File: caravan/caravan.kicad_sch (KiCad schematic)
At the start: 61 parts

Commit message: updated caravan
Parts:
- R?: value 680Ω -> 47Ω
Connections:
- new net: CB?.1, U?. (PE), U?.~ (PE)
- new net: CB?.3, U?. (PE), U?.~ (PE)
- new net: U?. (OUT-), U?. (PE) (x2)
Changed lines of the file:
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@@
   (title_block
     (title "Autark-Schaltplan")
-    (date "2024-10-14")
+    (date "2024-11-29")
     (comment 1 "Fendt Bianco Activ 390 FHS Autark-Schaltplan")
   )
@@
       (effects (font (size 1.27 1.27)) hide)
     )
-    (property "Value" "680Ω" (id 1) (at 304.165 211.1812 90))
+    (property "Value" "47Ω" (id 1) (at 304.165 211.1812 90))
     (property "Footprint" "" (id 2) (at 304.165 211.582 90)
       (effects (font (size 1.27 1.27)) hide)
@@
     )
     (path "/4729930f-060c-4c53-b9ff-46eeef07ff5b"
-      (reference "R?") (unit 1) (value "680Ω") (footprint "")
+      (reference "R?") (unit 1) (value "47Ω") (footprint "")
     )
     (path "/00000000-0000-0000-0000-000060e629cb"

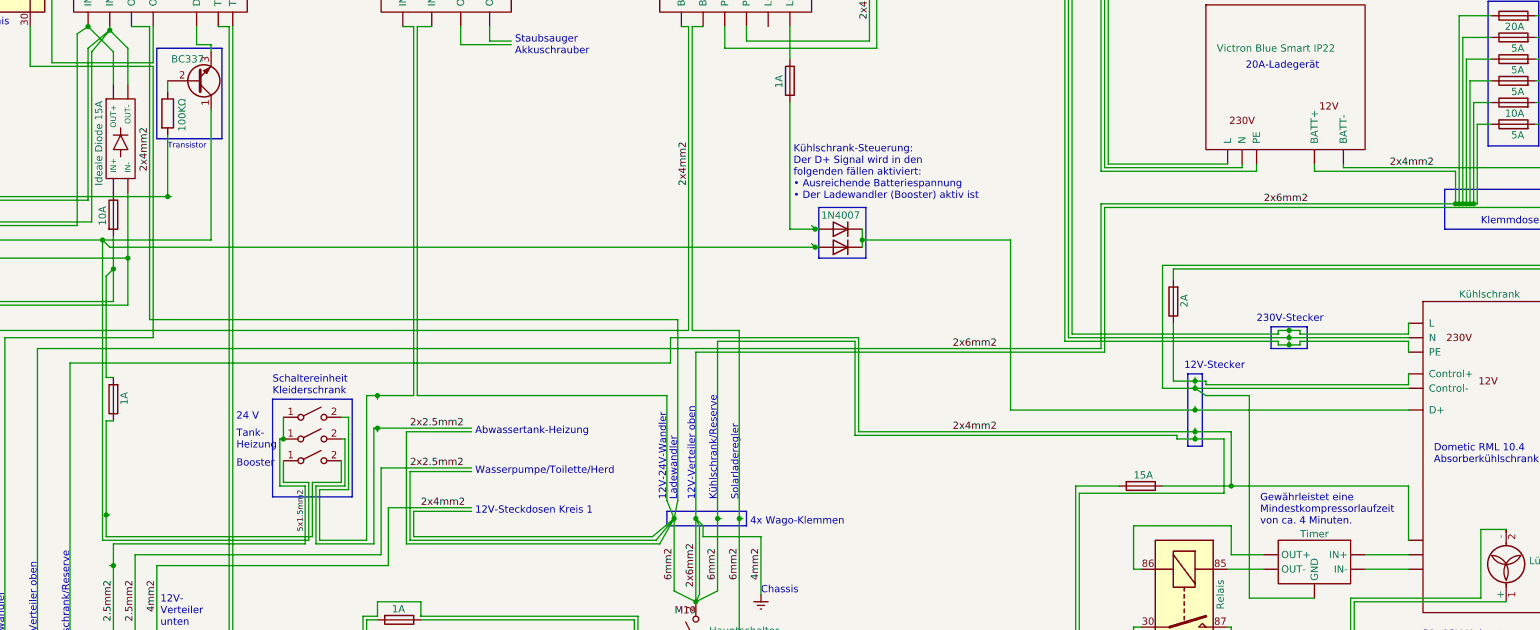
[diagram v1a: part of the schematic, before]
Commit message: Added 555-delay-opto
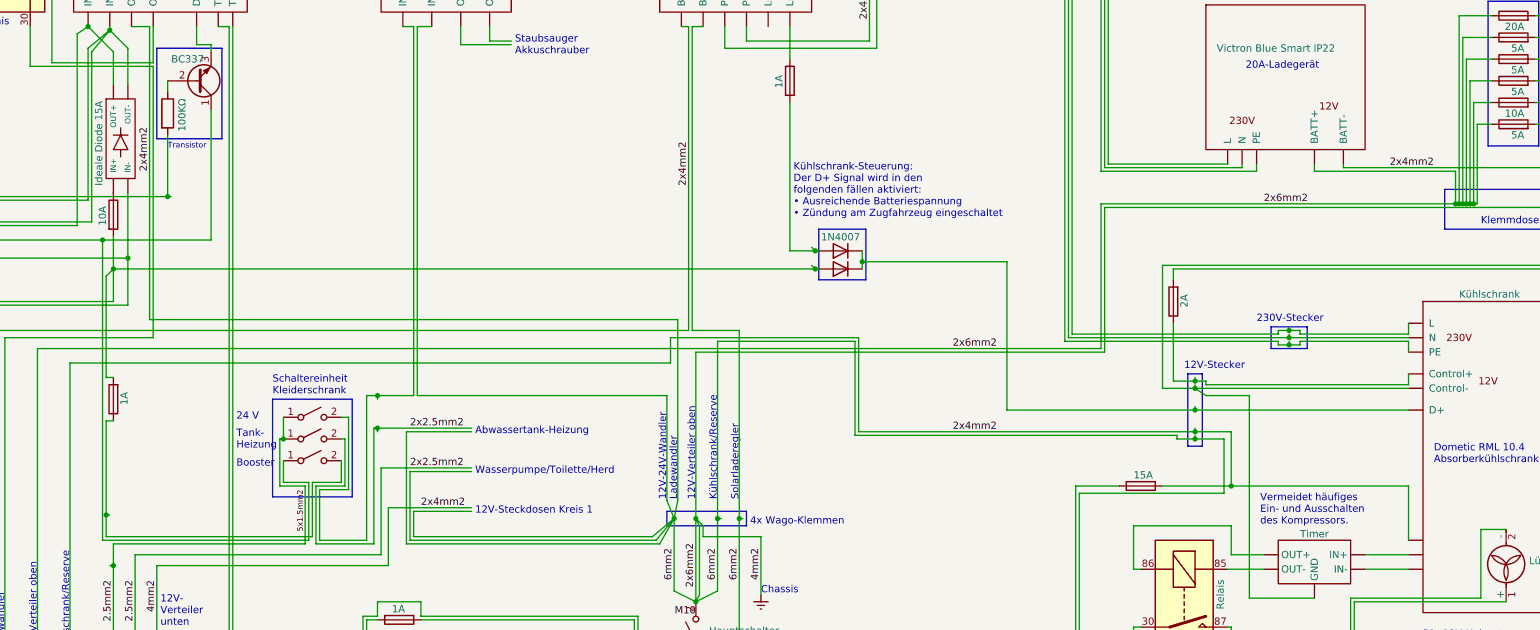
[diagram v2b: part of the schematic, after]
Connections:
- net Earth: now also D?.2 (A)
- net at K?.85, Q?.1 (C), SW?.1 (A): no longer D?.2 (A)
- new net: CB?.1, U?. (PE), U?.~ (PE)
- new net: CB?.3, U?. (PE), U?.~ (PE)
- new net: U?. (OUT-), U?. (PE) (x2)
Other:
- note added: "Kühlschrank-Steuerung: Der D+ Signal wird in den folgenden fällen aktiviert: • Ausreichende Batteriespannung • Zündung am Zugfahrzeug eingeschaltet"
- note added: "Vermeidet häufiges Ein- und Ausschalten des Kompressors."
- note removed: "Gewährleistet eine Mindestkompressorlaufzeit von ca. 4 Minuten."
- note removed: "Kühlschrank-Steuerung: Der D+ Signal wird in den folgenden fällen aktiviert: • Ausreichende Batteriespannung • Der Ladewandler (Booster) aktiv ist"
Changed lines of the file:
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@@
   (title_block
     (title "Autark-Schaltplan")
-    (date "2024-11-29")
+    (date "2025-01-06")
     (comment 1 "Fendt Bianco Activ 390 FHS Autark-Schaltplan")
   )
@@
   (junction (at 290.195 81.28) (diameter 0) (color 0 0 0 0)
   )
-  (junction (at 247.65 136.525) (diameter 0) (color 0 0 0 0)
+  (junction (at 247.65 140.335) (diameter 0) (color 0 0 0 0)
   )
   (junction (at 160.655 213.995) (diameter 0) (color 0 0 0 0)
@@
   (junction (at 146.05 171.45) (diameter 0) (color 0 0 0 0)
   )
-  (junction (at 239.395 137.795) (diameter 0) (color 0 0 0 0)
+  (junction (at 239.395 141.605) (diameter 0) (color 0 0 0 0)
   )
   (junction (at 108.585 212.725) (diameter 0) (color 0 0 0 0)
@@
   (junction (at 170.18 236.855) (diameter 0) (color 0 0 0 0)
   )
-  (junction (at 239.395 134.62) (diameter 0) (color 0 0 0 0)
+  (junction (at 239.395 138.43) (diameter 0) (color 0 0 0 0)
   )
   (junction (at 354.33 130.175) (diameter 0) (color 0 0 0 0)
@@
     (stroke (width 0) (type default) (color 0 0 0 0))
   )
-  (wire (pts (xy 238.76 137.16) (xy 239.395 137.795))
+  (wire (pts (xy 238.76 140.97) (xy 239.395 141.605))
     (stroke (width 0) (type default) (color 0 0 0 0))
   )
@@
     (stroke (width 0) (type default) (color 0 0 0 0))
   )
-  (wire (pts (xy 115.57 137.795) (xy 239.395 137.795))
-    (stroke (width 0) (type default) (color 0 0 0 0))
-  )
   (wire (pts (xy 332.74 213.36) (xy 332.74 213.995))
     (stroke (width 0) (type default) (color 0 0 0 0))
@@
     (stroke (width 0) (type default) (color 0 0 0 0))
   )
-  (wire (pts (xy 234.95 112.395) (xy 234.95 134.62))
+  (wire (pts (xy 234.95 112.395) (xy 234.95 138.43))
     (stroke (width 0) (type default) (color 0 0 0 0))
   )
@@
     (stroke (width 0) (type default) (color 0 0 0 0))
   )
-  (wire (pts (xy 273.685 136.525) (xy 273.685 166.37))
+  (wire (pts (xy 273.05 140.335) (xy 273.05 166.37))
     (stroke (width 0) (type default) (color 0 0 0 0))
   )
@@
     (stroke (width 0) (type default) (color 0 0 0 0))
   )
-  (wire (pts (xy 247.65 136.525) (xy 247.65 137.795))
+  (wire (pts (xy 247.65 140.335) (xy 247.65 141.605))
     (stroke (width 0) (type default) (color 0 0 0 0))
   )
@@
     (stroke (width 0) (type default) (color 0 0 0 0))
   )
-  (wire (pts (xy 273.685 166.37) (xy 306.07 166.37))
+  (wire (pts (xy 273.05 166.37) (xy 306.07 166.37))
     (stroke (width 0) (type default) (color 0 0 0 0))
   )
@@
     (stroke (width 0) (type default) (color 0 0 0 0))
   )
-  (wire (pts (xy 247.65 136.525) (xy 273.685 136.525))
+  (wire (pts (xy 247.65 140.335) (xy 273.05 140.335))
     (stroke (width 0) (type default) (color 0 0 0 0))
   )
@@
     (stroke (width 0) (type default) (color 0 0 0 0))
   )
+  (wire (pts (xy 116.205 141.605) (xy 239.395 141.605))
+    (stroke (width 0) (type default) (color 0 0 0 0))
+  )
   (wire (pts (xy 109.855 100.33) (xy 109.855 133.985))
     (stroke (width 0) (type default) (color 0 0 0 0))
@@
     (stroke (width 0) (type default) (color 0 0 0 0))
   )
-  (wire (pts (xy 247.65 134.62) (xy 247.65 136.525))
+  (wire (pts (xy 247.65 138.43) (xy 247.65 140.335))
     (stroke (width 0) (type default) (color 0 0 0 0))
   )
@@
     (stroke (width 0) (type default) (color 0 0 0 0))
   )
-  (wire (pts (xy 114.3 136.525) (xy 115.57 137.795))
-    (stroke (width 0) (type default) (color 0 0 0 0))
-  )
   (wire (pts (xy 222.25 154.305) (xy 246.38 154.305))
     (stroke (width 0) (type default) (color 0 0 0 0))
@@
     (stroke (width 0) (type default) (color 0 0 0 0))
   )
-  (polyline (pts (xy 240.03 130.81) (xy 240.03 139.7))
+  (polyline (pts (xy 240.03 134.62) (xy 240.03 143.51))
     (stroke (width 0) (type default) (color 0 0 0 0))
   )
@@
     (stroke (width 0) (type default) (color 0 0 0 0))
   )
-  (polyline (pts (xy 248.285 130.81) (xy 248.285 139.7))
+  (polyline (pts (xy 248.285 134.62) (xy 248.285 143.51))
     (stroke (width 0) (type default) (color 0 0 0 0))
   )
@@
     (stroke (width 0) (type default) (color 0 0 0 0))
   )
-  (wire (pts (xy 239.395 134.62) (xy 240.03 134.62))
+  (wire (pts (xy 239.395 138.43) (xy 240.03 138.43))
     (stroke (width 0) (type default) (color 0 0 0 0))
   )
@@
     (stroke (width 0) (type default) (color 0 0 0 0))
   )
-  (wire (pts (xy 238.76 133.985) (xy 239.395 134.62))
+  (wire (pts (xy 238.76 137.795) (xy 239.395 138.43))
     (stroke (width 0) (type default) (color 0 0 0 0))
   )
@@
     (stroke (width 0) (type default) (color 0 0 0 0))
   )
-  (wire (pts (xy 234.95 134.62) (xy 239.395 134.62))
+  (wire (pts (xy 234.95 138.43) (xy 239.395 138.43))
     (stroke (width 0) (type default) (color 0 0 0 0))
   )
@@
     (stroke (width 0) (type default) (color 0 0 0 0))
   )
-  (polyline (pts (xy 240.03 130.81) (xy 248.285 130.81))
+  (polyline (pts (xy 240.03 134.62) (xy 248.285 134.62))
     (stroke (width 0) (type default) (color 0 0 0 0))
   )
@@
     (stroke (width 0) (type default) (color 0 0 0 0))
   )
-  (polyline (pts (xy 248.285 139.7) (xy 240.03 139.7))
+  (polyline (pts (xy 248.285 143.51) (xy 240.03 143.51))
     (stroke (width 0) (type default) (color 0 0 0 0))
   )
@@
     (stroke (width 0) (type default) (color 0 0 0 0))
   )
-  (wire (pts (xy 239.395 137.795) (xy 240.03 137.795))
+  (wire (pts (xy 239.395 141.605) (xy 240.03 141.605))
     (stroke (width 0) (type default) (color 0 0 0 0))
   )
@@
     (effects (font (size 1.27 1.27)) (justify left bottom))
   )
-  (text "Gewährleistet eine \nMindestkompressorlaufzeit \nvon ca. 4 Minuten."
+  (text "Vermeidet häufiges \nEin- und Ausschalten \ndes Kompressors."
     (at 317.5 186.69 0)
     (effects (font (size 1.27 1.27)) (justify left bottom))
@@
     (effects (font (size 1.27 1.27)) (justify left bottom))
   )
-  (text "Kühlschrank-Steuerung:\nDer D+ Signal wird in den \nfolgenden fällen aktiviert:\n• Ausreichende Batteriespannung\n• Der Ladewandler (Booster) aktiv ist"
-    (at 235.585 129.54 0)
+  (text "Kühlschrank-Steuerung:\nDer D+ Signal wird in den \nfolgenden fällen aktiviert:\n• Ausreichende Batteriespannung\n• Zündung am Zugfahrzeug eingeschaltet"
+    (at 235.585 132.715 0)
     (effects (font (size 1.27 1.27)) (justify left bottom))
   )
@@
     (pin "2")
   )
-  (symbol (lib_id "Diode:1N4007") (at 243.84 137.795 180) (unit 1)
+  (symbol (lib_id "Diode:1N4007") (at 243.84 141.605 180) (unit 1)
     (in_bom yes) (on_board yes) (fields_autoplaced)
-    (property "Reference" "D?" (id 0) (at 243.84 132.8252 0)
+    (property "Reference" "D?" (id 0) (at 243.84 136.6352 0)
       (effects (font (size 1.27 1.27)) hide)
     )
-    (property "Value" "1N4007" (id 1) (at 243.84 135.3621 0)
+    (property "Value" "1N4007" (id 1) (at 243.84 139.1721 0)
       (effects (font (size 1.27 1.27)) hide)
     )
-    (property "Footprint" "Diode_THT:D_DO-41_SOD81_P10.16mm_Horizontal" (id 2) (at 243.84 133.35 0)
+    (property "Footprint" "Diode_THT:D_DO-41_SOD81_P10.16mm_Horizontal" (id 2) (at 243.84 137.16 0)
       (effects (font (size 1.27 1.27)) hide)
     )
-    (property "Datasheet" "http://www.vishay.com/docs/88503/1n4001.pdf" (id 3) (at 243.84 137.795 0)
+    (property "Datasheet" "http://www.vishay.com/docs/88503/1n4001.pdf" (id 3) (at 243.84 141.605 0)
       (effects (font (size 1.27 1.27)) hide)
     )
@@
     (pin "")
   )
-  (symbol (lib_id "Diode:1N4007") (at 243.84 134.62 180) (unit 1)
+  (symbol (lib_id "Diode:1N4007") (at 243.84 138.43 180) (unit 1)
     (in_bom yes) (on_board yes) (fields_autoplaced)
-    (property "Reference" "D?" (id 0) (at 243.84 129.6502 0)
+    (property "Reference" "D?" (id 0) (at 243.84 133.4602 0)
       (effects (font (size 1.27 1.27)) hide)
     )
-    (property "Value" "1N4007" (id 1) (at 243.84 132.1871 0))
-    (property "Footprint" "Diode_THT:D_DO-41_SOD81_P10.16mm_Horizontal" (id 2) (at 243.84 130.175 0)
+    (property "Value" "1N4007" (id 1) (at 243.84 135.9971 0))
+    (property "Footprint" "Diode_THT:D_DO-41_SOD81_P10.16mm_Horizontal" (id 2) (at 243.84 133.985 0)
       (effects (font (size 1.27 1.27)) hide)
     )
-    (property "Datasheet" "http://www.vishay.com/docs/88503/1n4001.pdf" (id 3) (at 243.84 134.62 0)
+    (property "Datasheet" "http://www.vishay.com/docs/88503/1n4001.pdf" (id 3) (at 243.84 138.43 0)
       (effects (font (size 1.27 1.27)) hide)
     )

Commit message: Updated caravan
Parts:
- removed K?: Relais, symbol caravan-rescue:Relay_Automotive_SPST-microfarad-de
- removed R?: 47Ω, symbol Device:R
- removed U?: Kühlschrank, symbol microfarad-de:Dometic_Fridge_2
- added U?: Dometic RML10.4, symbol microfarad-de:Dometic RML10
- M?: value Lüfter -> Kühlschrank-Lüfter
- U?: value Timer -> Drehzahlregler
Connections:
- net Earth: now also U?. (wh)
- net at CB?.1, U?.~ (PE): now also U?. (wh)
- net at CB?.3, U?.~ (PE): now also U?. (wh)
- net at F?.1: now also U?. (wh)
- net at D?.1 (K), D?.1 (K): now also U?. (wh)
- new net: U?. (T), U?. (T) (x2)
- new net: U?. (T), U?. (wh) (x2)
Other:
- note added: "Absorberkühlschrank- Steuergerät"
- note added: "Drehzahlregler-Schaltplan unter: github.com/microfarad-de/fridge-controller"
- note removed: "Dometic RML 10.4 Absorberkühlschrank"
- note removed: "Vermeidet häufiges Ein- und Ausschalten des Kompressors."

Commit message: Updated caravan
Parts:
- added F?: 1A, symbol Device:Fuse
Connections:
- net Earth: now also F?.2; no longer D?.2 (A)
- new net: CB?.1, U?. (wh), U?.~ (PE)
- new net: CB?.3, U?. (wh), U?.~ (PE)
- new net: D?.2 (A), F?.1
- new net: U?. (T), U?. (T) (x2)
- new net: U?. (T), U?. (wh) (x2)
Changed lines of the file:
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@@
   (title_block
     (title "Autark-Schaltplan")
-    (date "2025-03-21")
+    (date "2025-06-19")
     (comment 1 "Fendt Bianco Activ 390 FHS Autark-Schaltplan")
   )
@@
     (stroke (width 0) (type default) (color 0 0 0 0))
   )
-  (wire (pts (xy 116.205 141.605) (xy 239.395 141.605))
+  (wire (pts (xy 116.205 141.605) (xy 125.73 141.605))
     (stroke (width 0) (type default) (color 0 0 0 0))
   )
@@
     (stroke (width 0) (type default) (color 0 0 0 0))
   )
+  (wire (pts (xy 133.35 141.605) (xy 239.395 141.605))
+    (stroke (width 0) (type default) (color 0 0 0 0))
+  )
   (wire (pts (xy 116.205 193.675) (xy 116.205 205.105))
     (stroke (width 0) (type default) (color 0 0 0 0))
@@
     (pin "2")
   )
+  (symbol (lib_id "Device:Fuse") (at 129.54 141.605 270) (unit 1)
+    (in_bom yes) (on_board yes)
+    (property "Reference" "F?" (id 0) (at 130.7084 143.129 0)
+      (effects (font (size 1.27 1.27)) (justify left) hide)
+    )
+    (property "Value" "1A" (id 1) (at 128.27 139.7 90)
+      (effects (font (size 1.27 1.27)) (justify left))
+    )
+    (property "Footprint" "" (id 2) (at 129.54 139.827 90)
+      (effects (font (size 1.27 1.27)) hide)
+    )
+    (property "Datasheet" "~" (id 3) (at 129.54 141.605 0)
+      (effects (font (size 1.27 1.27)) hide)
+    )
+    (pin "1")
+    (pin "2")
+  )
   (symbol (lib_id "microfarad-de:555_Delay") (at 327.914 185.674 0) (unit 1)
     (in_bom yes) (on_board yes)
@@
       (reference "F?") (unit 1) (value "20A") (footprint "")
     )
+    (path "/2cfda12a-94d3-44c5-814b-25b98cbb6186"
+      (reference "F?") (unit 1) (value "1A") (footprint "")
+    )
     (path "/c38dd4a9-859c-423b-a4c4-6138f440c395"

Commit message: Updated caravan
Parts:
- removed F?: 1A, symbol Device:Fuse
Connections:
- new net: CB?.1, U?. (wh), U?.~ (PE)
- new net: CB?.3, U?. (wh), U?.~ (PE)
- new net: U?. (T), U?. (T) (x2)
- new net: U?. (T), U?. (wh) (x2)
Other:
- note added: "Kühlschrank-Steuerung: Der D+ Signal wird von folgenden Quellen erzeugt: • Kühlschrank-Steuerung vom Raspberry Pi • Zündung am Zugfahrzeug eingeschaltet"
- note added: "Raspberry Pi (Victron Cerbo GX)"
- note removed: "Kühlschrank-Steuerung: Der D+ Signal wird in den folgenden fällen aktiviert: • Ausreichende Batteriespannung • Zündung am Zugfahrzeug eingeschaltet"
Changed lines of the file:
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@@
   (title_block
     (title "Autark-Schaltplan")
-    (date "2025-06-19")
+    (date "2025-07-28")
     (comment 1 "Fendt Bianco Activ 390 FHS Autark-Schaltplan")
   )
@@
     (stroke (width 0) (type default) (color 0 0 0 0))
   )
+  (wire (pts (xy 213.36 138.43) (xy 239.395 138.43))
+    (stroke (width 0) (type default) (color 0 0 0 0))
+  )
   (wire (pts (xy 306.07 160.655) (xy 306.07 161.29))
     (stroke (width 0) (type default) (color 0 0 0 0))
@@
     (stroke (width 0) (type default) (color 0 0 0 0))
   )
-  (wire (pts (xy 234.95 99.06) (xy 234.95 104.775))
-    (stroke (width 0) (type default) (color 0 0 0 0))
-  )
   (wire (pts (xy 146.05 233.68) (xy 153.035 233.68))
     (stroke (width 0) (type default) (color 0 0 0 0))
@@
     (stroke (width 0) (type default) (color 0 0 0 0))
   )
-  (wire (pts (xy 234.95 112.395) (xy 234.95 138.43))
-    (stroke (width 0) (type default) (color 0 0 0 0))
-  )
   (wire (pts (xy 91.44 99.06) (xy 91.44 139.7))
     (stroke (width 0) (type default) (color 0 0 0 0))
@@
     (stroke (width 0) (type default) (color 0 0 0 0))
   )
-  (wire (pts (xy 234.95 138.43) (xy 239.395 138.43))
-    (stroke (width 0) (type default) (color 0 0 0 0))
-  )
   (wire (pts (xy 302.895 170.815) (xy 302.895 171.45))
     (stroke (width 0) (type default) (color 0 0 0 0))
@@
     (effects (font (size 1.27 1.27)) (justify left bottom))
   )
+  (text "Raspberry Pi\n(Victron Cerbo GX)" (at 193.675 139.065 0)
+    (effects (font (size 1.27 1.27)) (justify left bottom))
+  )
   (text "Booster" (at 137.795 176.53 0)
     (effects (font (size 1.27 1.27)) (justify left bottom))
@@
     (effects (font (size 1.27 1.27)) (justify left bottom))
   )
-  (text "Kühlschrank-Steuerung:\nDer D+ Signal wird in den \nfolgenden fällen aktiviert:\n• Ausreichende Batteriespannung\n• Zündung am Zugfahrzeug eingeschaltet"
-    (at 235.585 132.715 0)
+  (text "Kühlschrank-Steuerung:\nDer D+ Signal wird von folgenden Quellen erzeugt:\n• Kühlschrank-Steuerung vom Raspberry Pi\n• Zündung am Zugfahrzeug eingeschaltet"
+    (at 226.06 132.715 0)
     (effects (font (size 1.27 1.27)) (justify left bottom))
   )
@@
     (pin "2")
   )
-  (symbol (lib_id "Device:Fuse") (at 234.95 108.585 0) (unit 1)
-    (in_bom yes) (on_board yes)
-    (property "Reference" "F?" (id 0) (at 236.474 107.4166 0)
-      (effects (font (size 1.27 1.27)) (justify left) hide)
-    )
-    (property "Value" "1A" (id 1) (at 233.045 109.855 90)
-      (effects (font (size 1.27 1.27)) (justify left))
-    )
-    (property "Footprint" "" (id 2) (at 233.172 108.585 90)
-      (effects (font (size 1.27 1.27)) hide)
-    )
-    (property "Datasheet" "~" (id 3) (at 234.95 108.585 0)
-      (effects (font (size 1.27 1.27)) hide)
-    )
-    (pin "1")
-    (pin "2")
-  )
   (symbol (lib_id "Motor:Fan") (at 359.156 210.82 90) (unit 1)
     (in_bom yes) (on_board yes)
@@
       (reference "F?") (unit 1) (value "1A") (footprint "")
     )
-    (path "/c38dd4a9-859c-423b-a4c4-6138f440c395"
-      (reference "F?") (unit 1) (value "1A") (footprint "")
-    )

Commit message: Updated caravan - fridge rewire
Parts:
- removed D?: LED, symbol Device:LED
- removed F?: 2A, symbol Device:Fuse
- removed F?: 15A, symbol Device:Fuse
- removed M?: Kühlschrank-Lüfter, symbol Motor:Fan
- removed M?: Lüfter, symbol Motor:Fan
- removed U?: Drehzahlregler, symbol microfarad-de:555_Delay
- removed U?: Isotherm Kühlaggregat, symbol microfarad-de:Isotherm
- removed U?: Dometic RML10.4, symbol microfarad-de:Dometic RML10
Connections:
- net Earth: now also CB?.1
- net Kühlschrank N: now reaches U?.~ (PE)
- net Kühlschrank N: now also CB?.3; no longer CB?.1
- net Kühlschrank +: now reaches F?.2
- net Absorber -: now reaches F?.1, K?.86, U?.~ (OUT-)
- net Kühlschrank D+: now reaches D?.1 (K), D?.1 (K)
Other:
- added sheet Fridge (fridge.kicad_sch)
- note added: "Hinweise zum Votronic Ladewandler: Das Relais unterbindet den Rückladezweig und verhindert damit das Einschalten des ATC ohne Zugfahrzeug. Die Transistorschaltung aktiviert den Ladevorgang nur, wenn ATC-Schaltplus und Zugfahrzeug-D+ beide aktiv sind. Dadurch wird der Ladevorgang unterbrochen, wenn der Motor aus ist oder die ATC-Bremse aktiv ist. Die ideale Diode ermöglicht das gleichzeitige Nutze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"
- note added: "Transistor- Schaltung"
- note removed: "12V-Stecker"
- note removed: "230V-Stecker"
- note removed: "Absorberkühlschrank- Steuergerät"
- note removed: "Die 12V-Heizpatrone wurde deaktiviert und durch das Isotherm Kompressor-Kühlaggregat ersetzt."
- note removed: "Draußen"
- note removed: "Drehzahlregler-Schaltplan unter: github.com/microfarad-de/fridge-controller"
- note removed: "Hinweise zum Votronic Ladewandler: Das Relais unterbindet den Rückladezweig und verhindert damit das Einschalten des ATC ohne Zugfahrzeug. Der Transistor aktiviert den Ladevorgang nur, wenn ATC-Schaltplus und Zugfahrzeug-D+ beide aktiv sind. Dadurch wird der Ladevorgang unterbrochen, wenn der Motor aus ist oder die ATC-Bremse aktiv ist. Die ideale Diode ermöglicht das gleichzeitige Nutzen der Sch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"
- note removed: "Secop BD35F Kompressor"
- note removed: "Transistor"
